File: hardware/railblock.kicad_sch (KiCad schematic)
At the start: 38 parts, among them J1 8P8C, J2 8P8C, J3 Conn_01x08_Socket, J4 Conn_01x03_Socket, J5 Conn_01x03_Socket, J6 Conn_01x03_Socket, U1 PESD2CAN, U2 MCP2562-E-SN, U3 ESP32-WROOM-32, U4 ULN2003A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

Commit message: feat: Make hall and relais working
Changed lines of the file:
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@@
 (kicad_sch
-	(version 20231120)
+	(version 20250114)
 	(generator "eeschema")
-	(generator_version "8.0")
+	(generator_version "9.0")
 	(paper "A4")
 	(junction
@@
 		)
 	)
+	(embedded_fonts no)
 )

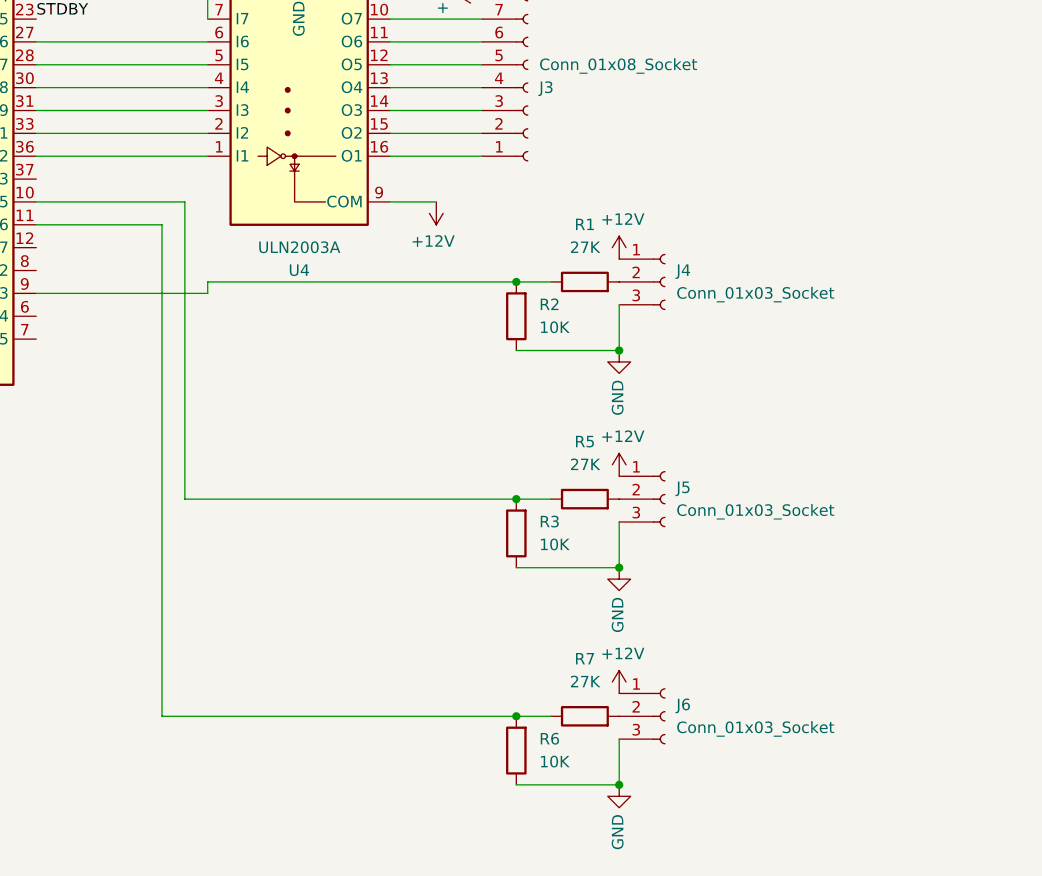
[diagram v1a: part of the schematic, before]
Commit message: fix: Add pull-up for hall sensors
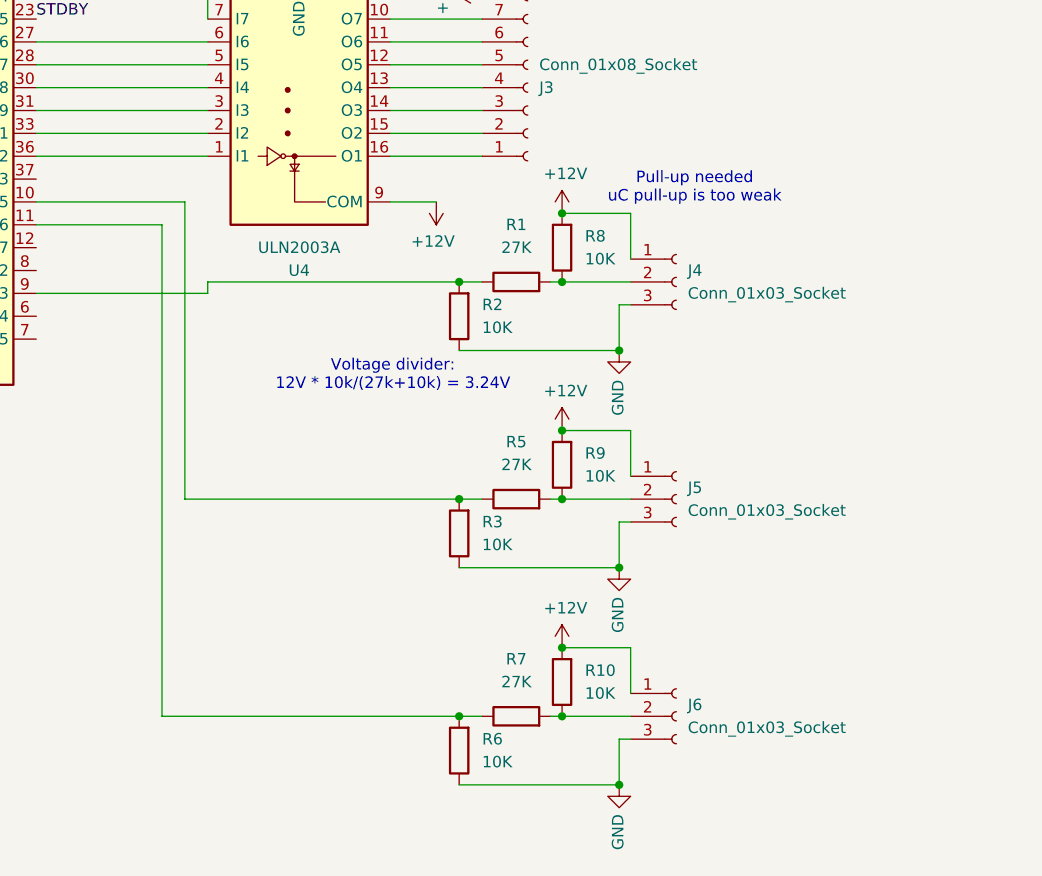
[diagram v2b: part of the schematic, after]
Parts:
- added R10, R8, R9: 10K, Resistor_SMD:R_0603_1608Metric_Pad0.98x0.95mm_HandSolder, symbol Device:R
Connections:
- net +12V: now also R10.2, R8.2, R9.2
- net at J4.2 (Pin_2), R1.2: now also R8.1
- net at J6.2 (Pin_2), R7.2: now also R10.1
- net at J5.2 (Pin_2), R5.2: now also R9.1
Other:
- note added: "Pull-up needed uC pull-up is too weak"
- note added: "Voltage divider: 12V * 10k/(27k+10k) = 3.24V"
- moved on the sheet: J4, J5, J6, R1, R2, R3, R5, R6, R7

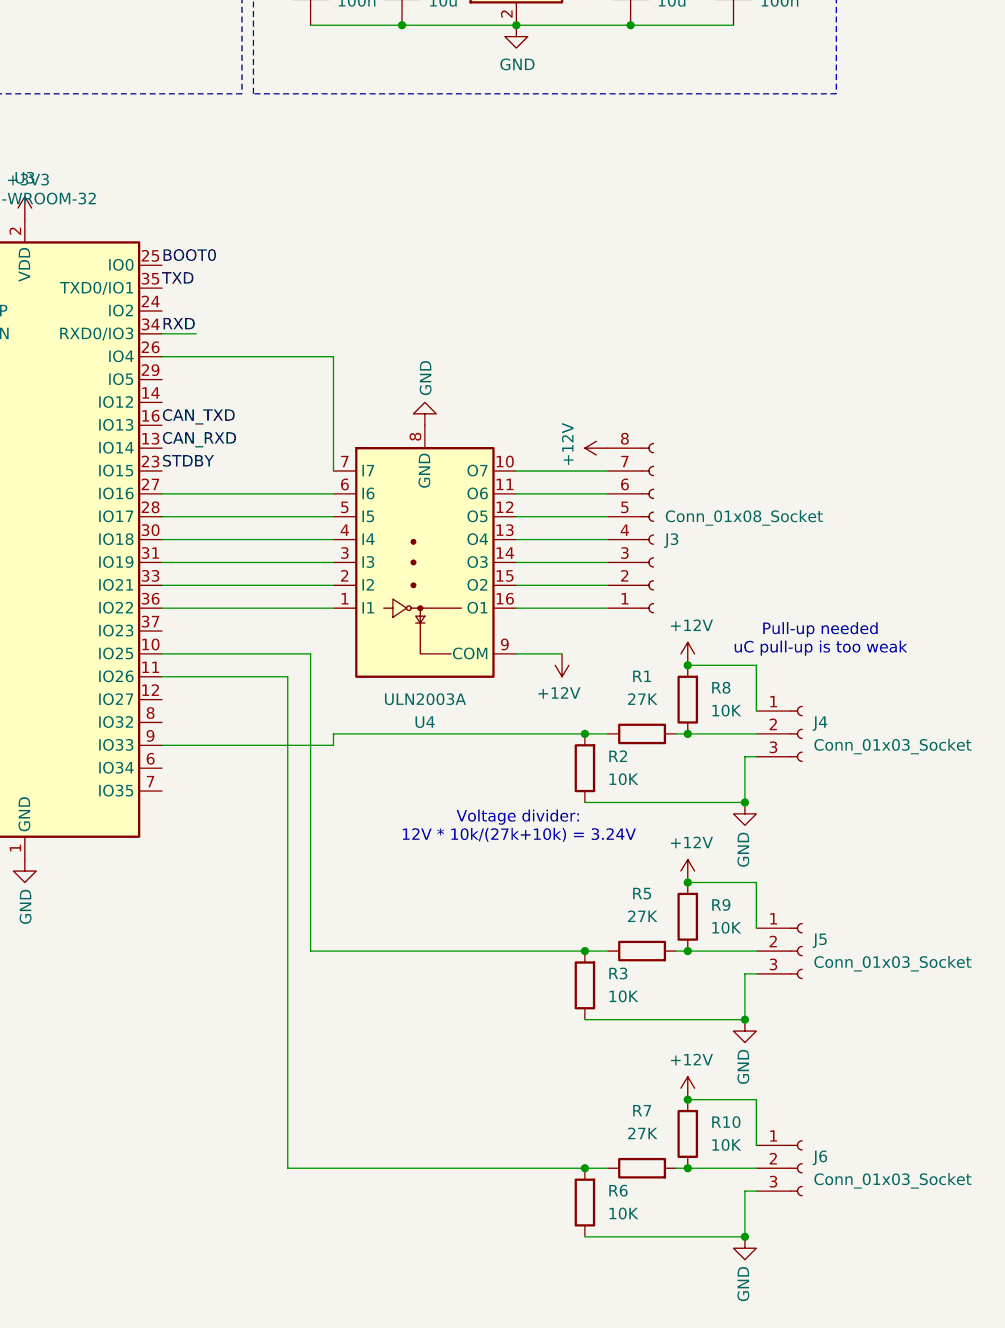
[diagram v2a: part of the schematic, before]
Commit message: feat: Add JTAG interface
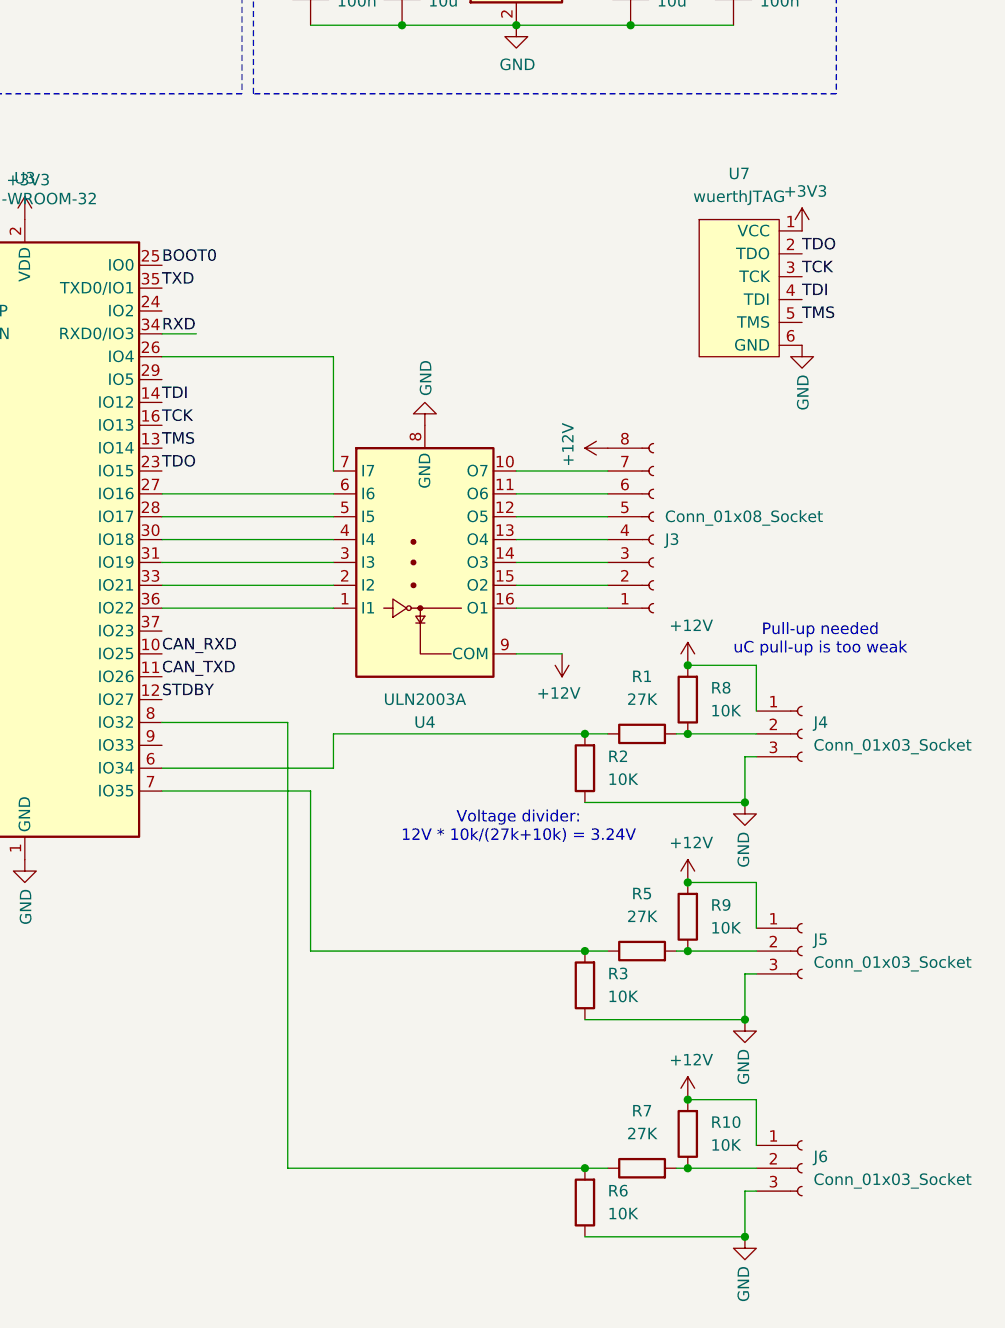
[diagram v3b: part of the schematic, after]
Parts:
- added U7: wuerthJTAG, awesome:wuerthJTAG, symbol awesome:wuerthJTAG
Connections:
- net +3V3: now also U7.1 (VCC)
- net CAN_RXD: now also U3.10 (IO25); no longer U3.13 (IO14)
- net CAN_TXD: now also U3.11 (IO26); no longer U3.16 (IO13)
- net GND: now also U7.6 (GND)
- net STDBY: now also U3.12 (IO27); no longer U3.23 (IO15)
- net at R3.2, R5.1: now also U3.7 (IO35); no longer U3.10 (IO25)
- net at R6.2, R7.1: now also U3.8 (IO32); no longer U3.11 (IO26)
- net TDI: now reaches U3.14 (IO12)
- net TDI: now also U7.4 (TDI)
- net at U3.6 (IO34): now also R1.1, R2.2
- new net TCK: U3.16 (IO13), U7.3 (TCK)
- new net TDO: U3.23 (IO15), U7.2 (TDO)
- new net TMS: U3.13 (IO14), U7.5 (TMS)
- now unconnected: U3.9 (IO33)

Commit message: feat: Bring more structure into the project
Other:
- note added: "SPDX-License-Identifier: CERN-OHL-S-2.0"
- title: (none) -> Railblock
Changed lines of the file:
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@@
 	(generator_version "9.0")
 	(paper "A4")
+	(title_block
+		(title "Railblock")
+	)
+	(text "SPDX-License-Identifier: CERN-OHL-S-2.0"
+		(exclude_from_sim no)
+		(at 221.234 163.83 0)
+		(effects
+			(font
+				(size 1.27 1.27)
+			)
+		)
+	)
 	(text "Voltage divider:\n12V * 10k/(27k+10k) = 3.24V"
 		(exclude_from_sim no)
@@
 		)
 		(stroke
-			(width 0)
-			(type default)
-		)
-	)
-	(wire
-		(pts
-			(xy 213.36 162.56) (xy 260.35 162.56)
-		)
-		(stroke
